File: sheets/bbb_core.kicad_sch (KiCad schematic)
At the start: 11 parts, among them P10 BeagleBone_Black_Header, P11 BeagleBone_Black_Header, SW2 SW_DIP_x02, U2 CAT24C256

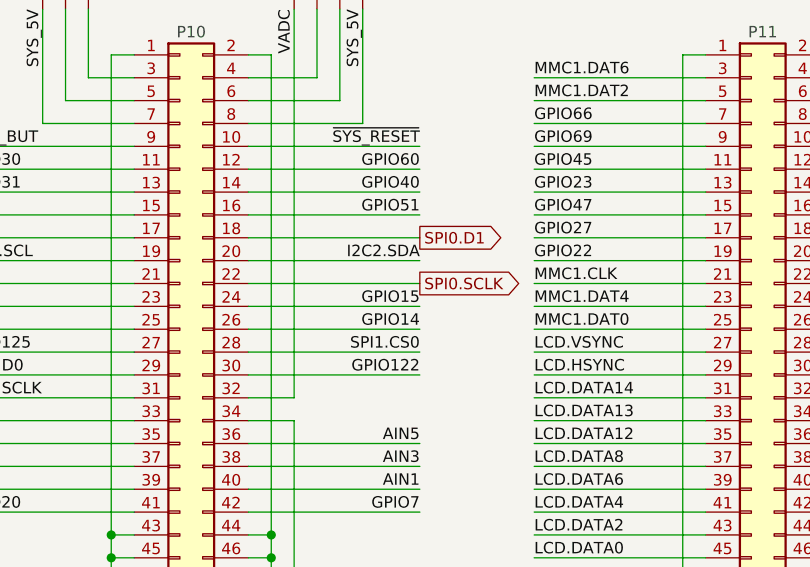
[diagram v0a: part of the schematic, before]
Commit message: CDH Updated to have Payload USB interface and Trigger connectors
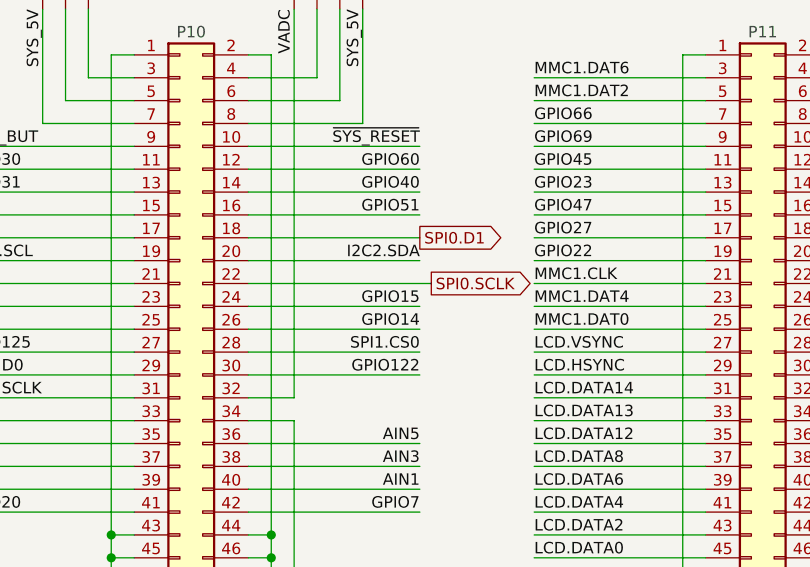
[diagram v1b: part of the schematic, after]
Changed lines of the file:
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@@
 	(wire
 		(pts
-			(xy 116.84 58.42) (xy 135.89 58.42)
+			(xy 116.84 58.42) (xy 137.16 58.42)
 		)
 		(stroke
@@
 	(global_label "SPI0.SCLK"
 		(shape output)
-		(at 135.89 58.42 0)
+		(at 137.16 58.42 0)
 		(fields_autoplaced yes)
 		(effects
@@
 		)
 		(property "Intersheetrefs" "${INTERSHEET_REFS}"
-			(at 148.6465 58.42 0)
+			(at 149.9165 58.42 0)
 			(hide yes)
 			(show_name no)

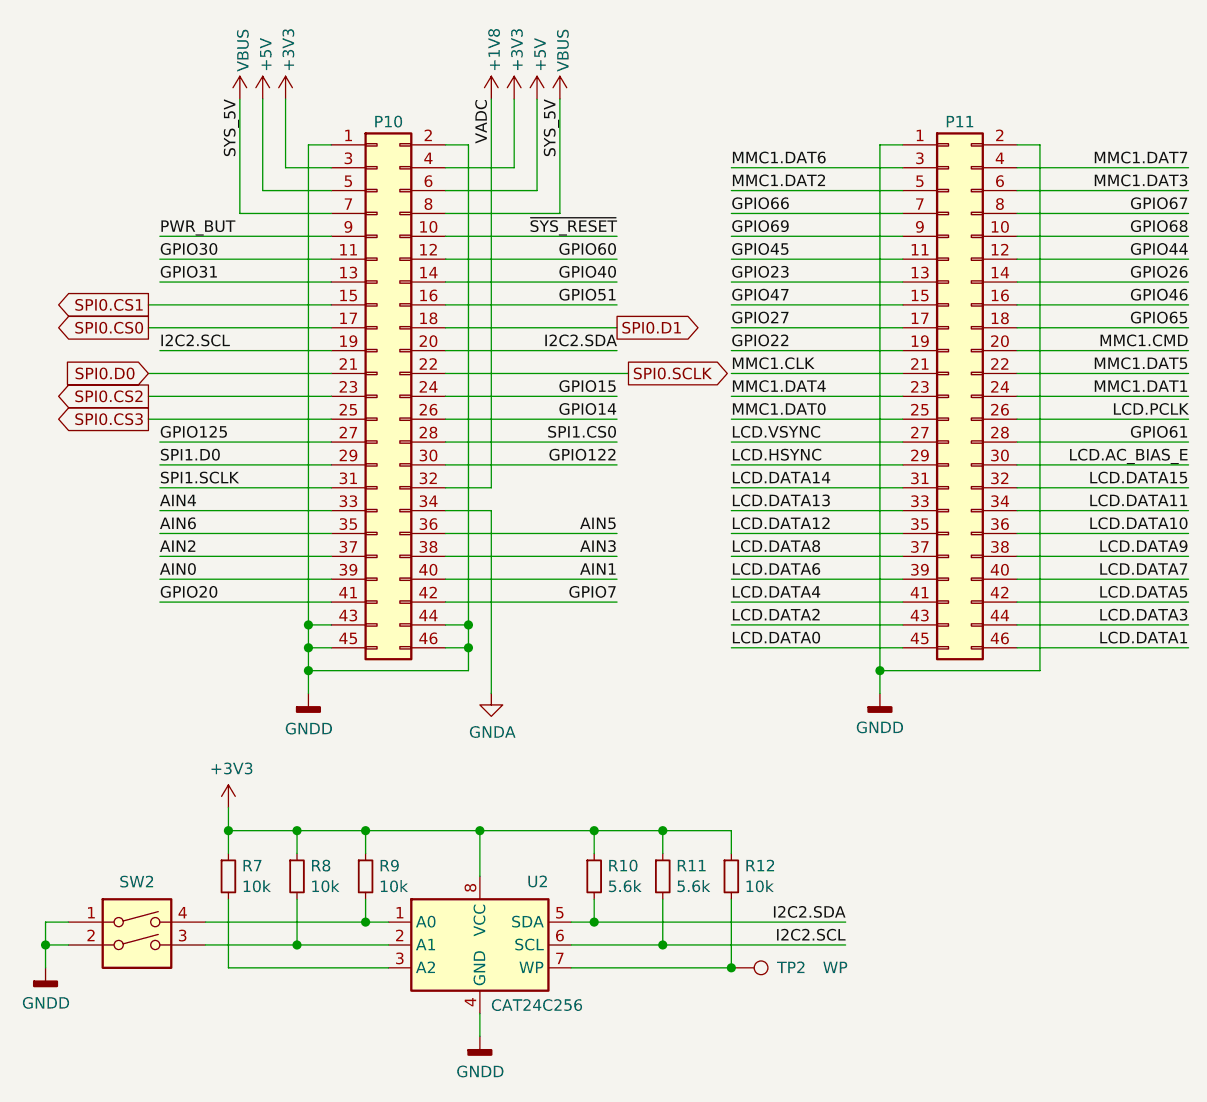
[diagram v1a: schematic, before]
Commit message: Payload USB updated to have 4 USB 2.0 Hub
Added support for USB flash or eUSB flash for storage.
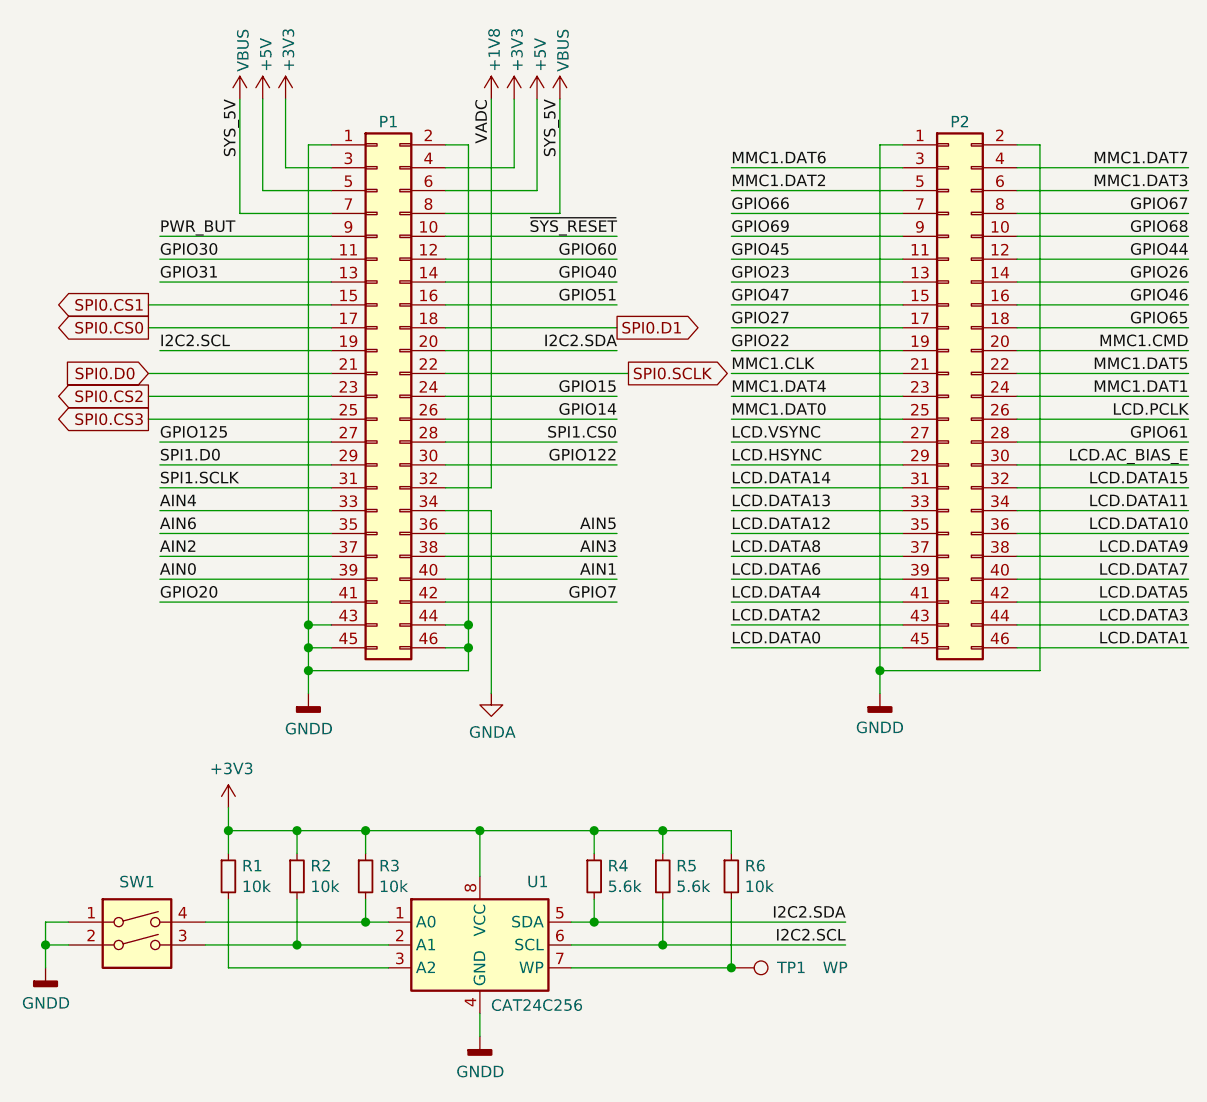
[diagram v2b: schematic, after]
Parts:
- renumbered P10 to P1, P11 to P2, R7 to R1, R8 to R2, R9 to R3, R10 to R4, R11 to R5, R12 to R6, SW2 to SW1, TP2 to TP1, U2 to U1
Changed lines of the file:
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@@
 		(in_pos_files yes)
 		(dnp no)
-		(property "Reference" "P10"
+		(property "Reference" "P1"
 			(at 110.49 30.48 0)
 			(show_name no)
@@
 			(project "hs2-cdh-pcb"
 				(path "/e63e39d7-6ac0-4ffd-8aa3-1841a4541b55/b9a16af5-117f-430a-90b4-e04345c94fab"
-					(reference "P10")
+					(reference "P1")
 					(unit 1)
 				)
@@
 		(in_pos_files yes)
 		(dnp no)
-		(property "Reference" "#PWR0114"
+		(property "Reference" "#PWR08"
 			(at 121.92 31.75 0)
 			(hide yes)
@@
 			(project "hs2-cdh-pcb"
 				(path "/e63e39d7-6ac0-4ffd-8aa3-1841a4541b55/b9a16af5-117f-430a-90b4-e04345c94fab"
-					(reference "#PWR0114")
+					(reference "#PWR08")
 					(unit 1)
 				)
@@
 		(in_pos_files yes)
 		(dnp no)
-		(property "Reference" "TP2"
+		(property "Reference" "TP1"
 			(at 153.67 124.46 90)
 			(show_name no)
@@
 			(project "hs2-cdh-pcb"
 				(path "/e63e39d7-6ac0-4ffd-8aa3-1841a4541b55/b9a16af5-117f-430a-90b4-e04345c94fab"
-					(reference "TP2")
+					(reference "TP1")
 					(unit 1)
 				)
@@
 		(in_pos_files yes)
 		(dnp no)
-		(property "Reference" "R11"
+		(property "Reference" "R5"
 			(at 142.4687 113.1506 0)
 			(show_name no)
@@
 			(project "hs2-cdh-pcb"
 				(path "/e63e39d7-6ac0-4ffd-8aa3-1841a4541b55/b9a16af5-117f-430a-90b4-e04345c94fab"
-					(reference "R11")
+					(reference "R5")
 					(unit 1)
 				)
@@
 		(in_pos_files yes)
 		(dnp no)
-		(property "Reference" "#PWR05"
+		(property "Reference" "#PWR013"
 			(at 165.1 100.33 0)
 			(hide yes)
@@
 			(project "hs2-cdh-pcb"
 				(path "/e63e39d7-6ac0-4ffd-8aa3-1841a4541b55/b9a16af5-117f-430a-90b4-e04345c94fab"
-					(reference "#PWR05")
+					(reference "#PWR013")
 					(unit 1)
 				)
@@
 		(in_pos_files yes)
 		(dnp no)
-		(property "Reference" "#PWR013"
+		(property "Reference" "#PWR011"
 			(at 127 31.75 0)
 			(hide yes)
@@
 			(project "hs2-cdh-pcb"
 				(path "/e63e39d7-6ac0-4ffd-8aa3-1841a4541b55/b9a16af5-117f-430a-90b4-e04345c94fab"
-					(reference "#PWR013")
+					(reference "#PWR011")
 					(unit 1)
 				)
@@
 		(in_pos_files yes)
 		(dnp no)
-		(property "Reference" "SW2"
+		(property "Reference" "SW1"
 			(at 82.55 114.9286 0)
 			(show_name no)
@@
 			(project "hs2-cdh-pcb"
 				(path "/e63e39d7-6ac0-4ffd-8aa3-1841a4541b55/b9a16af5-117f-430a-90b4-e04345c94fab"
-					(reference "SW2")
+					(reference "SW1")
 					(unit 1)
 				)
@@
 		(in_pos_files yes)
 		(dnp no)
-		(property "Reference" "#PWR0110"
+		(property "Reference" "#PWR02"
 			(at 92.71 110.49 0)
 			(hide yes)
@@
 			(project "hs2-cdh-pcb"
 				(path "/e63e39d7-6ac0-4ffd-8aa3-1841a4541b55/b9a16af5-117f-430a-90b4-e04345c94fab"
-					(reference "#PWR0110")
+					(reference "#PWR02")
 					(unit 1)
 				)
@@
 		(in_pos_files yes)
 		(dnp no)
-		(property "Reference" "#PWR012"
+		(property "Reference" "#PWR010"
 			(at 124.46 31.75 0)
 			(hide yes)
@@
 			(project "hs2-cdh-pcb"
 				(path "/e63e39d7-6ac0-4ffd-8aa3-1841a4541b55/b9a16af5-117f-430a-90b4-e04345c94fab"
-					(reference "#PWR012")
+					(reference "#PWR010")
 					(unit 1)
 				)
@@
 		(in_pos_files yes)
 		(dnp no)
-		(property "Reference" "#PWR0109"
+		(property "Reference" "#PWR01"
 			(at 72.39 130.81 0)
 			(hide yes)
@@
 			(project "hs2-cdh-pcb"
 				(path "/e63e39d7-6ac0-4ffd-8aa3-1841a4541b55/b9a16af5-117f-430a-90b4-e04345c94fab"
-					(reference "#PWR0109")
+					(reference "#PWR01")
 					(unit 1)
 				)
@@
 		(in_pos_files yes)
 		(dnp no)
-		(property "Reference" "R10"
+		(property "Reference" "R4"
 			(at 134.8487 113.1506 0)
 			(show_name no)
@@
 			(project "hs2-cdh-pcb"
 				(path "/e63e39d7-6ac0-4ffd-8aa3-1841a4541b55/b9a16af5-117f-430a-90b4-e04345c94fab"
-					(reference "R10")
+					(reference "R4")
 					(unit 1)
 				)
@@
 		(in_pos_files yes)
 		(dnp no)
-		(property "Reference" "R8"
+		(property "Reference" "R2"
 			(at 101.8287 113.1506 0)
 			(show_name no)
@@
 			(project "hs2-cdh-pcb"
 				(path "/e63e39d7-6ac0-4ffd-8aa3-1841a4541b55/b9a16af5-117f-430a-90b4-e04345c94fab"
-					(reference "R8")
+					(reference "R2")
 					(unit 1)
 				)
@@
 		(in_pos_files yes)
 		(dnp no)
-		(property "Reference" "R9"
+		(property "Reference" "R3"
 			(at 109.4487 113.1506 0)
 			(show_name no)
@@
 			(project "hs2-cdh-pcb"
 				(path "/e63e39d7-6ac0-4ffd-8aa3-1841a4541b55/b9a16af5-117f-430a-90b4-e04345c94fab"
-					(reference "R9")
+					(reference "R3")
 					(unit 1)
 				)
@@
 		(in_pos_files yes)
 		(dnp no)
-		(property "Reference" "#PWR0112"
+		(property "Reference" "#PWR06"
 			(at 101.6 100.33 0)
 			(hide yes)
@@
 			(project "hs2-cdh-pcb"
 				(path "/e63e39d7-6ac0-4ffd-8aa3-1841a4541b55/b9a16af5-117f-430a-90b4-e04345c94fab"
-					(reference "#PWR0112")
+					(reference "#PWR06")
 					(unit 1)
 				)
@@
 		(in_pos_files yes)
 		(dnp no)
-		(property "Reference" "#PWR010"
+		(property "Reference" "#PWR04"
 			(at 96.52 31.75 0)
 			(hide yes)
@@
 			(project "hs2-cdh-pcb"
 				(path "/e63e39d7-6ac0-4ffd-8aa3-1841a4541b55/b9a16af5-117f-430a-90b4-e04345c94fab"
-					(reference "#PWR010")
+					(reference "#PWR04")
 					(unit 1)
 				)
@@
 		(in_pos_files yes)
 		(dnp no)
-		(property "Reference" "P11"
+		(property "Reference" "P2"
 			(at 173.99 30.48 0)
 			(show_name no)
@@
 			(project "hs2-cdh-pcb"
 				(path "/e63e39d7-6ac0-4ffd-8aa3-1841a4541b55/b9a16af5-117f-430a-90b4-e04345c94fab"
-					(reference "P11")
+					(reference "P2")
 					(unit 1)
 				)
@@
 		(in_pos_files yes)
 		(dnp no)
-		(property "Reference" "#PWR0111"
+		(property "Reference" "#PWR03"
 			(at 93.98 31.75 0)
 			(hide yes)
@@
 			(project "hs2-cdh-pcb"
 				(path "/e63e39d7-6ac0-4ffd-8aa3-1841a4541b55/b9a16af5-117f-430a-90b4-e04345c94fab"
-					(reference "#PWR0111")
+					(reference "#PWR03")
 					(unit 1)
 				)
@@
 		(in_pos_files yes)
 		(dnp no)
-		(property "Reference" "#PWR0115"
+		(property "Reference" "#PWR09"
 			(at 121.92 100.33 0)
 			(hide yes)
@@
 			(project "hs2-cdh-pcb"
 				(path "/e63e39d7-6ac0-4ffd-8aa3-1841a4541b55/b9a16af5-117f-430a-90b4-e04345c94fab"
-					(reference "#PWR0115")
+					(reference "#PWR09")
 					(unit 1)
 				)
@@
 		(in_pos_files yes)
 		(dnp no)
-		(property "Reference" "R7"
+		(property "Reference" "R1"
 			(at 94.2087 113.1506 0)
 			(show_name no)
@@
 			(project "hs2-cdh-pcb"
 				(path "/e63e39d7-6ac0-4ffd-8aa3-1841a4541b55/b9a16af5-117f-430a-90b4-e04345c94fab"
-					(reference "R7")
+					(reference "R1")
 					(unit 1)
 				)
@@
 		(in_pos_files yes)
 		(dnp no)
-		(property "Reference" "#PWR011"
+		(property "Reference" "#PWR05"
 			(at 99.06 31.75 0)
 			(hide yes)
@@
 			(project "hs2-cdh-pcb"
 				(path "/e63e39d7-6ac0-4ffd-8aa3-1841a4541b55/b9a16af5-117f-430a-90b4-e04345c94fab"
-					(reference "#PWR011")
+					(reference "#PWR05")
 					(unit 1)
 				)
@@
 		(in_pos_files yes)
 		(dnp no)
-		(property "Reference" "U2"
+		(property "Reference" "U1"
 			(at 128.27 114.9096 0)
 			(show_name no)
@@
 			(project "hs2-cdh-pcb"
 				(path "/e63e39d7-6ac0-4ffd-8aa3-1841a4541b55/b9a16af5-117f-430a-90b4-e04345c94fab"
-					(reference "U2")
+					(reference "U1")
 					(unit 1)
 				)
@@
 		(in_pos_files yes)
 		(dnp no)
-		(property "Reference" "#PWR0113"
+		(property "Reference" "#PWR07"
 			(at 120.65 138.43 0)
 			(hide yes)
@@
 			(project "hs2-cdh-pcb"
 				(path "/e63e39d7-6ac0-4ffd-8aa3-1841a4541b55/b9a16af5-117f-430a-90b4-e04345c94fab"
-					(reference "#PWR0113")
+					(reference "#PWR07")
 					(unit 1)
 				)
@@
 		(in_pos_files yes)
 		(dnp no)
-		(property "Reference" "#PWR0116"
+		(property "Reference" "#PWR012"
 			(at 129.54 31.75 0)
 			(hide yes)
@@
 			(project "hs2-cdh-pcb"
 				(path "/e63e39d7-6ac0-4ffd-8aa3-1841a4541b55/b9a16af5-117f-430a-90b4-e04345c94fab"
-					(reference "#PWR0116")
+					(reference "#PWR012")
 					(unit 1)
 				)
@@
 		(in_pos_files yes)
 		(dnp no)
-		(property "Reference" "R12"
+		(property "Reference" "R6"
 			(at 150.0887 113.1506 0)
 			(show_name no)
@@
 			(project "hs2-cdh-pcb"
 				(path "/e63e39d7-6ac0-4ffd-8aa3-1841a4541b55/b9a16af5-117f-430a-90b4-e04345c94fab"
-					(reference "R12")
-					(unit 1)
-				)
+					(reference "R6")
+					(unit 1)
+				)
